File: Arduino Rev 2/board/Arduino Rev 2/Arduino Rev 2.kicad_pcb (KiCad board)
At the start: 2 copper layers, 25 parts, among them J401 10103594-0001LF, J601 Conn_01x12_Female, J602 Conn_01x12_Female, U201 ATMEGA328-AU, U401 FT231XS-U, Y301 ECS-160-20-30B-AGL-TR

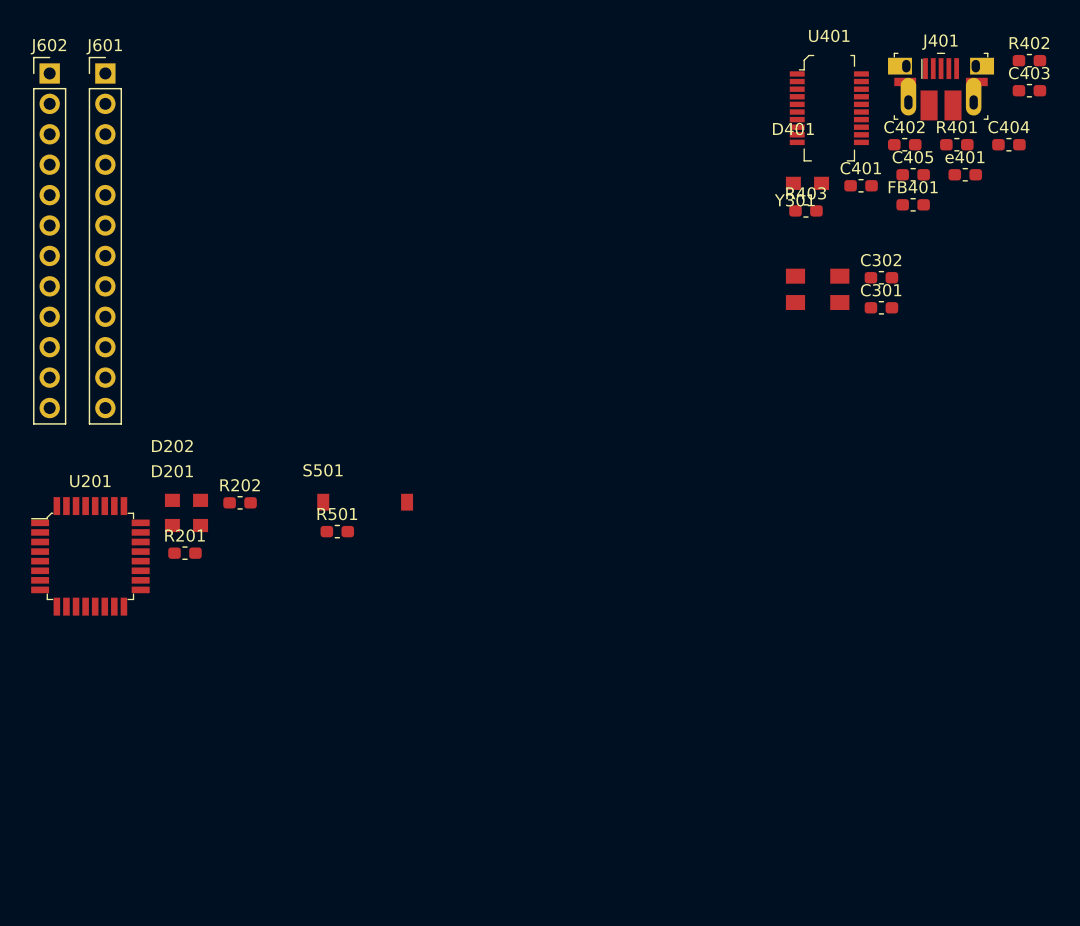
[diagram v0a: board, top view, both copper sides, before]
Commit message: Fixed Schematic. Routing Finished
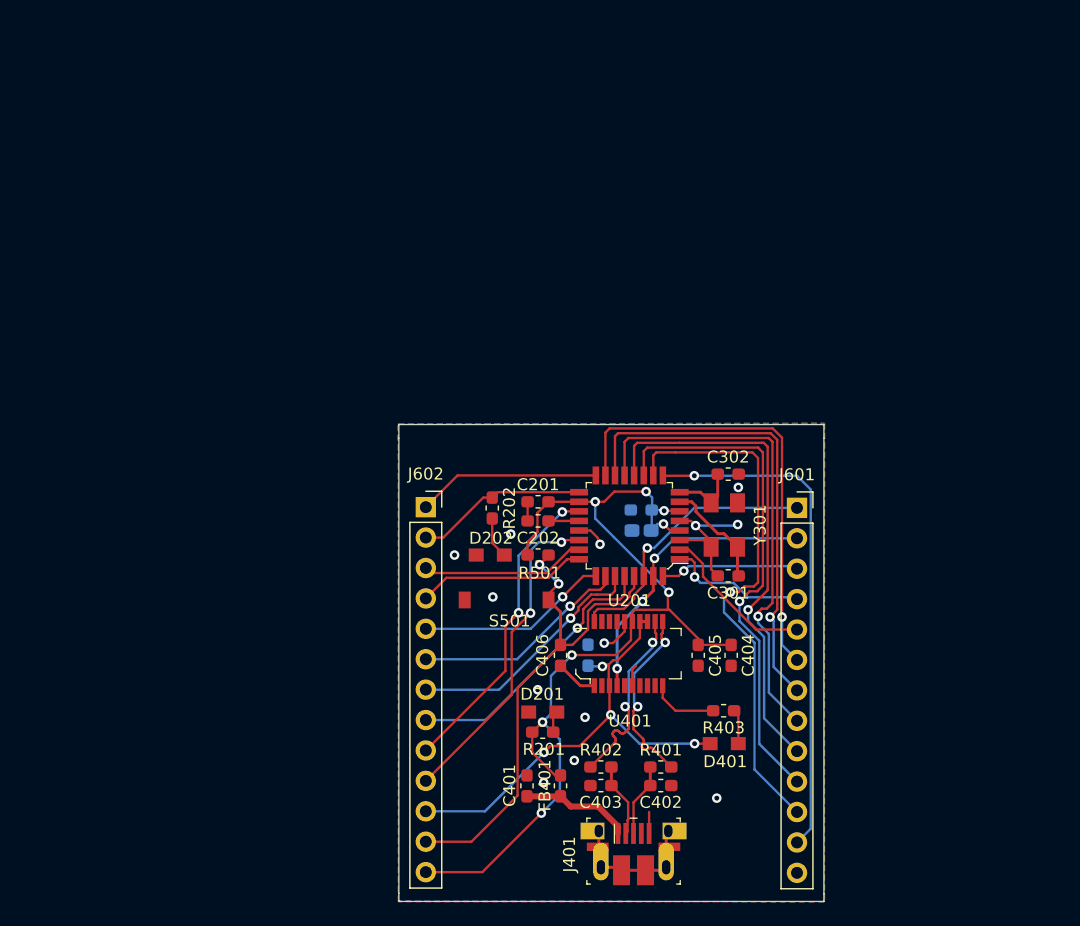
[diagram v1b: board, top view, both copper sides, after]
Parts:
- removed e401: 100nF, Arduino Rev 2:C_0603_1608Metric_Pad1.05x0.95mm_HandSolder
- added C201: 100 nF, Arduino Rev 2:C_0603_1608Metric_Pad1.05x0.95mm_HandSolder, F.Cu at (154.6, 102.8)
- added C202: 100 nF, Arduino Rev 2:C_0603_1608Metric_Pad1.05x0.95mm_HandSolder, F.Cu at (154.6, 104.4)
- added C203: 4.7 uF, Arduino Rev 2:CP_EIA-1608-10_AVX-L_Pad1.25x1.05mm_HandSolder, B.Cu at (163.3, 105.2)
- added C204: 100 nF, Arduino Rev 2:C_0603_1608Metric_Pad1.05x0.95mm_HandSolder, B.Cu at (163.2, 103.5)
- added C406: 100 nF, Arduino Rev 2:C_0603_1608Metric_Pad1.05x0.95mm_HandSolder, F.Cu at (156.5, 115.6)
- added C407: 100nF, Arduino Rev 2:C_0603_1608Metric_Pad1.05x0.95mm_HandSolder, B.Cu at (158.8, 115.6)
- J601, J602: footprint Arduino Rev 2:PinHeader_1x12_P2.54mm_Vertical -> Arduino Rev 2:PinSocket_1x13_P2.54mm_Vertical
- moved R402 69.0 mm to (159.9, 125.0)
- moved J401 68.8 mm to (162.6, 133.3)
- moved J601 68.2 mm to (176.2, 103.3)
- moved C403 68.2 mm to (159.9, 126.5), turned to 180 degrees
- moved R401 57.6 mm to (164.9, 125.0), turned to 180 degrees
- moved C401 57.4 mm to (153.7, 126.5), turned to 270 degrees
- moved C402 57.3 mm to (164.9, 126.5)
- moved FB401 56.8 mm to (156.5, 126.5), turned to 270 degrees
- moved C404 48.5 mm to (170.8, 115.6), turned to 270 degrees
- moved U401 48.5 mm to (162.2, 115.5), turned to 90 degrees
- moved J602 47.9 mm to (145.2, 103.2)
- moved D401 47.0 mm to (171.3, 123.0), turned to 180 degrees
- moved U201 45.1 mm to (162.2, 104.8), turned to 180 degrees
- moved C405 44.0 mm to (168.0, 115.6), turned to 270 degrees
- moved R403 42.3 mm to (170.1, 120.2), turned to 180 degrees
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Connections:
- net /USB TO UART/DM renamed /USB TO UART/D-
- net /USB TO UART/DP renamed /USB TO UART/D+
- net Net-(R401-Pad1) renamed /USB TO UART/d2+
- net Net-(R402-Pad1) renamed /USB TO UART/d2-
- J601 pad 10: /PIN HEADERS/10 -> /PIN HEADERS/8
- J601 pad 11: /PIN HEADERS/11 -> /PIN HEADERS/7
- J601 pad 12: /PIN HEADERS/12 -> /PIN HEADERS/6
- J601 pad 6: /PIN HEADERS/6 -> /PIN HEADERS/12
- J601 pad 7: /PIN HEADERS/7 -> /PIN HEADERS/11
- J601 pad 8: /PIN HEADERS/8 -> /PIN HEADERS/10
- J602 pad 11: /PIN HEADERS/23 -> +3V3
- U201 pad 20: /PIN HEADERS/23 -> /ATMega328/AREF
- U401 pad 1: /RESET -> Net-(C406-Pad2)
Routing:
- net +5V: track 0.00 -> 85.0 mm, vias 0 -> 8
- net /PIN HEADERS/7: track 0.00 -> 44.9 mm, vias 0 -> 1
- net /PIN HEADERS/8: track 0.00 -> 42.9 mm, vias 0 -> 1
- net /PIN HEADERS/6: track 0.00 -> 42.8 mm, vias 0 -> 1
- net /RESET: track 0.00 -> 42.8 mm, vias 0 -> 2
- net /PIN HEADERS/9: track 0.00 -> 41.7 mm, vias 0 -> 1
- net /PIN HEADERS/10: track 0.00 -> 40.8 mm, vias 0 -> 1
- net +3V3: track 0.00 -> 39.7 mm, vias 0 -> 4
- net /PIN HEADERS/11: track 0.00 -> 39.3 mm, vias 0 -> 1
- net /PIN HEADERS/12: track 0.00 -> 37.9 mm, vias 0 -> 1
- net /PIN HEADERS/22: track 0.00 -> 27.3 mm, vias 0 -> 2
- net /PIN HEADERS/21: track 0.00 -> 26.1 mm, vias 0 -> 2
- net /D1_TX: track 0.00 -> 24.5 mm, vias 0 -> 3
- net GND: track 0.00 -> 23.4 mm, vias 0 -> 13
- net /PIN HEADERS/20: track 0.00 -> 23.1 mm, vias 0 -> 1
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- added copper zone on B.Cu, net GND
- added copper zone on F.Cu, net GND
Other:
- board outline added: 35.5 x 39.8 mm
- net class Default: trace_width 0.25 -> 0.2
